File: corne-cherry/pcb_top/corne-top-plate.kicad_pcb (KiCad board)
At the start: 2 copper layers, 132.9 x 91.4 mm, 5 parts

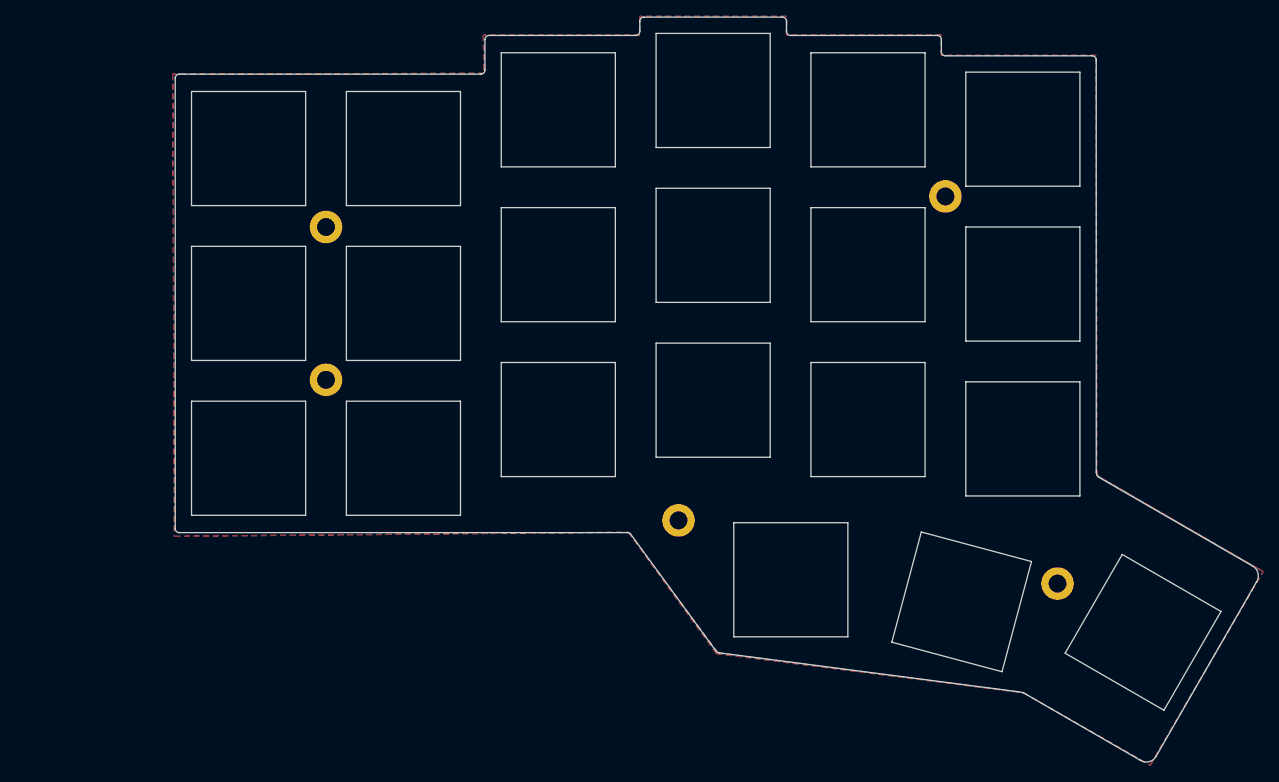
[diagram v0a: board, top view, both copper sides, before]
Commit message: added PCB top plate
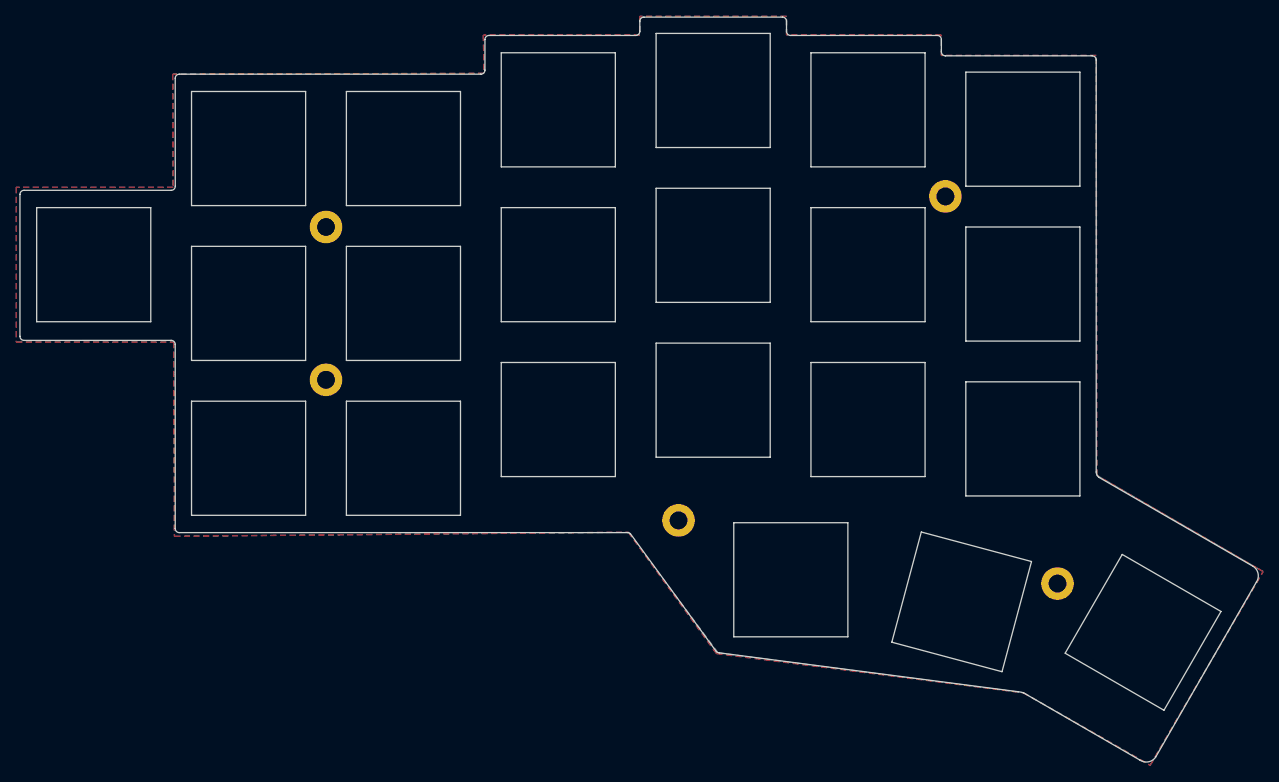
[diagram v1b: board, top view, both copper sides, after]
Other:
- board size 132.9 x 91.4 mm -> 151.9 x 91.4 mm
- board text added: "Jorne Keyboard PCB Designed by Joric"
- board text removed: "Corne Keyboard PCB Designed by foostan"
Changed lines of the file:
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@@
-(kicad_pcb (version 20171130) (host pcbnew "(5.0.0-3-g5ebb6b6)")
+(kicad_pcb (version 20171130) (host pcbnew "(5.1.0)-1")
   (general
     (thickness 1.6)
-    (drawings 125)
+    (drawings 137)
     (tracks 0)
     (zones 0)
@@
     (zone_45_only no)
     (trace_min 0.2)
-    (segment_width 0.1)
-    (edge_width 0.15)
     (via_size 0.6)
     (via_drill 0.4)
@@
     (uvia_min_size 0.2)
     (uvia_min_drill 0.1)
+    (edge_width 0.15)
+    (segment_width 0.1)
     (pcb_text_width 0.3)
     (pcb_text_size 1.5 1.5)
@@
     (pad_to_mask_clearance 0.2)
     (aux_axis_origin 174 65.7)
-    (grid_origin 129.53 123.035)
-    (visible_elements FFFFFF7F)
+    (grid_origin 101 84.375)
+    (visible_elements 7FFFFFFF)
     (pcbplotparams
       (layerselection 0x010f0_ffffffff)
-      (usegerberextensions false)
+      (usegerberextensions true)
       (usegerberattributes false)
       (usegerberadvancedattributes false)
@@
     (pad "" thru_hole circle (at 0 0) (size 4 4) (drill 2.2) (layers *.Cu *.Mask))
   )
+  (gr_line (start 44 98.375) (end 44 84.375) (layer Edge.Cuts) (width 0.15))
+  (gr_line (start 44 98.375) (end 58 98.375) (layer Edge.Cuts) (width 0.15))
+  (gr_line (start 44 84.375) (end 58 84.375) (layer Edge.Cuts) (width 0.15))
+  (gr_line (start 58 84.375) (end 58 98.375) (layer Edge.Cuts) (width 0.15))
+  (gr_line (start 61 123.75) (end 60.9996 101.1603) (angle 90) (layer Edge.Cuts) (width 0.15))
   (gr_line (start 189.31 133.925) (end 177.19 126.925) (layer Edge.Cuts) (width 0.15))
   (gr_line (start 182.31 146.045) (end 189.31 133.925) (layer Edge.Cuts) (width 0.15))
@@
   (gr_arc (start 174.847282 116.785192) (end 173.997282 116.810192) (angle -52.52752939) (layer Edge.Cuts) (width 0.15))
   (gr_arc (start 192.500001 129.550001) (end 193.65 130.325) (angle -90.22347501) (layer Edge.Cuts) (width 0.15))
-  (gr_line (start 193.275 128.4) (end 174.35 117.475) (layer Edge.Cuts) (width 0.15))
+  (gr_line (start 193.270509 128.396988) (end 174.35 117.475) (layer Edge.Cuts) (width 0.15))
   (gr_line (start 63 84.125) (end 63 70.125) (layer Edge.Cuts) (width 0.15))
   (gr_line (start 77 70.125) (end 77 84.125) (layer Edge.Cuts) (width 0.15))
   (gr_arc (start 180.14425 151.010957) (end 179.369251 152.160956) (angle -90.22347501) (layer Edge.Cuts) (width 0.15))
   (gr_arc (start 164.087404 147.16844) (end 165.075 143.9) (angle -11.21335546) (layer Edge.Cuts) (width 0.15))
-  (gr_line (start 181.3 151.775) (end 193.65 130.325) (layer Edge.Cuts) (width 0.15))
-  (gr_line (start 165.075 143.9) (end 179.4 152.175) (layer Edge.Cuts) (width 0.15))
-  (gr_line (start 127.75 139) (end 164.45 143.775) (layer Edge.Cuts) (width 0.15))
+  (gr_line (start 181.297263 151.781465) (end 193.65 130.325) (layer Edge.Cuts) (width 0.15))
+  (gr_line (start 165.075 143.9) (end 179.369251 152.160956) (layer Edge.Cuts) (width 0.15))
+  (gr_line (start 127.75 139) (end 164.420556 143.770344) (layer Edge.Cuts) (width 0.15))
   (gr_arc (start 127.75 138.5) (end 127.75 139) (angle 45) (layer Edge.Cuts) (width 0.15))
-  (gr_line (start 116.85 124.4) (end 127.4 138.85) (angle 90) (layer Edge.Cuts) (width 0.15))
+  (gr_line (start 116.853553 124.396447) (end 127.396447 138.853553) (angle 90) (layer Edge.Cuts) (width 0.15))
   (gr_line (start 169.26 130.5) (end 169.25 130.5) (angle 90) (layer Eco2.User) (width 2.5))
   (gr_line (start 122.76 122.75) (end 122.75 122.75) (angle 90) (layer Eco2.User) (width 2.5))
@@
   (gr_line (start 79.5 105.5) (end 79.51 105.5) (angle 90) (layer Eco2.User) (width 2.5))
   (gr_line (start 79.5 86.75) (end 79.51 86.75) (angle 90) (layer Eco2.User) (width 2.5))
-  (gr_text "Corne Keyboard\nPCB Designed by foostan" (at 118.11 121.445) (layer B.Mask)
+  (gr_text "Jorne Keyboard\nPCB Designed by Joric" (at 118.11 121.445) (layer B.Mask)
     (effects (font (size 1 1) (thickness 0.125)) (justify left mirror))
   )
-  (gr_text "Corne Keyboard\nPCB Designed by foostan" (at 98.74 121.445) (layer F.Mask)
+  (gr_text "Jorne Keyboard\nPCB Designed by Joric" (at 98.74 121.445) (layer F.Mask)
     (effects (font (size 1 1) (thickness 0.125)) (justify left))
   )
-  (gr_line (start 174 66.25) (end 174 116.825) (angle 90) (layer Edge.Cuts) (width 0.15))
+  (gr_line (start 174 66.25) (end 173.997282 116.810192) (angle 90) (layer Edge.Cuts) (width 0.15))
   (gr_arc (start 173.5 66.25) (end 173.5 65.75) (angle 90) (layer Edge.Cuts) (width 0.15))
   (gr_arc (start 116.5 124.75) (end 116.5 124.25) (angle 45) (layer Edge.Cuts) (width 0.15))
-  (gr_arc (start 61.5 123.75) (end 61.5 124.25) (angle 90) (layer Edge.Cuts) (width 0.15))
   (gr_arc (start 61.5 68.5) (end 61 68.5) (angle 90) (layer Edge.Cuts) (width 0.15))
   (gr_arc (start 98.5 67.5) (end 99 67.5) (angle 90) (layer Edge.Cuts) (width 0.15))
@@
   (gr_arc (start 154.5 63.75) (end 154.5 63.25) (angle 90) (layer Edge.Cuts) (width 0.15))
   (gr_arc (start 155.5 65.25) (end 155.5 65.75) (angle 90) (layer Edge.Cuts) (width 0.15))
-  (gr_line (start 116.5 124.25) (end 61.475 124.25) (angle 90) (layer Edge.Cuts) (width 0.15))
-  (gr_line (start 61 68.5) (end 61 123.75) (angle 90) (layer Edge.Cuts) (width 0.15))
-  (gr_line (start 98.5 68) (end 61.474992 68) (angle 90) (layer Edge.Cuts) (width 0.15))
+  (gr_line (start 116.5 124.25) (end 61.5 124.25) (angle 90) (layer Edge.Cuts) (width 0.15))
+  (gr_line (start 98.5 68) (end 61.5 68) (angle 90) (layer Edge.Cuts) (width 0.15))
   (gr_line (start 99 63.75) (end 99 67.5) (angle 90) (layer Edge.Cuts) (width 0.15))
   (gr_line (start 117.5 63.25) (end 99.5 63.25) (angle 90) (layer Edge.Cuts) (width 0.15))
@@
   (gr_line (start 155 65.25) (end 155 63.75) (angle 90) (layer Edge.Cuts) (width 0.15))
   (gr_line (start 173.5 65.75) (end 155.5 65.75) (angle 90) (layer Edge.Cuts) (width 0.15))
+  (gr_line (start 61 68.5) (end 61.0043 81.75) (angle 90) (layer Edge.Cuts) (width 0.15))
+  (gr_arc (start 61.5 123.75) (end 61.5 124.25) (angle 90) (layer Edge.Cuts) (width 0.15))
+  (gr_arc (start 42.4496 100.165) (end 41.9496 100.165) (angle -90) (layer Edge.Cuts) (width 0.15))
+  (gr_line (start 42.4496 82.25) (end 60.5043 82.25) (angle 90) (layer Edge.Cuts) (width 0.15))
+  (gr_line (start 42.4496 100.665) (end 60.4996 100.6603) (angle 90) (layer Edge.Cuts) (width 0.15))
+  (gr_arc (start 42.4496 82.75) (end 41.9496 82.75) (angle 90) (layer Edge.Cuts) (width 0.15))
+  (gr_line (start 41.9496 100.165) (end 41.9496 82.75) (angle 90) (layer Edge.Cuts) (width 0.15))
+  (gr_arc (start 60.4996 101.1603) (end 60.4996 100.6603) (angle 90) (layer Edge.Cuts) (width 0.15))
+  (gr_arc (start 60.5043 81.75) (end 61.0043 81.75) (angle 90) (layer Edge.Cuts) (width 0.15))
   (zone (net 0) (net_name "") (layer B.Cu) (hatch edge 0.508)
     (connect_pads (clearance 0.508))
@@
         (xy 174.075 117.225) (xy 174 67.9) (xy 174 65.7) (xy 155 65.7) (xy 155 63.2)
         (xy 136 63.2) (xy 136 60.9) (xy 118 60.9) (xy 118 63.2) (xy 98.8 63.2)
-        (xy 98.9 67.9) (xy 60.7 68) (xy 60.9 124.7) (xy 116.6 124.2) (xy 127.6 139)
-        (xy 165.075 143.9) (xy 180.625 152.8) (xy 194.475 129.025) (xy 194.075 128.8)
+        (xy 98.9 67.9) (xy 60.7 68) (xy 60.750702 81.875) (xy 41.5 81.875) (xy 41.5 100.875)
+        (xy 60.816942 100.875638) (xy 60.9 124.7) (xy 116.6 124.2) (xy 127.6 139) (xy 165.075 143.9)
+        (xy 180.625 152.8) (xy 194.475 129.025) (xy 194.075 128.8)
       )
     )
@@
         (xy 174.075 117.225) (xy 174 67.9) (xy 174 65.7) (xy 155 65.7) (xy 155 63.2)
         (xy 136 63.2) (xy 136 60.9) (xy 118 60.9) (xy 118 63.2) (xy 98.8 63.2)
-        (xy 98.9 67.9) (xy 60.7 68) (xy 60.9 124.7) (xy 116.6 124.2) (xy 127.4 139.1)
-        (xy 165.05 143.9) (xy 180.625 152.8) (xy 194.475 129.025) (xy 193.7 128.575)
+        (xy 98.9 67.9) (xy 60.7 68) (xy 60.748938 81.874121) (xy 41.5 81.875) (xy 41.5 100.875)
+        (xy 60.815963 100.875649) (xy 60.9 124.7) (xy 116.6 124.2) (xy 127.4 139.1) (xy 165.05 143.9)
+        (xy 180.625 152.8) (xy 194.475 129.025) (xy 193.7 128.575)
       )
     )
@@
       )
     )
+  )
+  (zone (net 0) (net_name "") (layers F&B.Cu) (hatch edge 0.508)
+    (connect_pads (clearance 0.508))
+    (min_thickness 0.254)
+    (keepout (tracks not_allowed) (vias not_allowed) (copperpour not_allowed))
+    (fill (arc_segments 16) (thermal_gap 0.508) (thermal_bridge_width 0.508))
+    (polygon
+      (pts
+        (xy 44 84.375) (xy 44 98.375) (xy 58 98.375) (xy 58 84.375)
+      )
+    )
